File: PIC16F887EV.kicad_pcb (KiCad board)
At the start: 2 copper layers, 45 parts, among them J1 Conn_01x05_Socket, P1 USB_C_Plug_USB2.0, SW1 SW_Push, SW10 SW_Push, SW11 SW_Push, SW12 SW_Push, SW13 SW_Push, SW14 SW_Push, SW15 SW_Push, SW16 SW_Push, SW2 SW_Push, SW3 SW_Push, SW4 SW_Push, SW5 SW_Push, SW6 SW_Push, SW7 SW_Push, SW8 SW_Push, SW9 SW_Push, U1 PIC16F887-IP, U2 FT230XS, U3 MMBT2222A-7-F

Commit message: Displays
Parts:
- added R7: 10K, Resistor_SMD:R_1206_3216Metric_Pad1.30x1.75mm_HandSolder, F.Cu at (110.2, 116.1)
- added R8: 10K, Resistor_SMD:R_1206_3216Metric_Pad1.30x1.75mm_HandSolder, F.Cu at (110.2, 119.4)
- added RV1: R_Potentiometer, Potentiometer_SMD:Potentiometer_ACP_CA6-VSMD_Vertical, F.Cu at (132.1, 124.5)
- added SW17: SW_Push, Button_Switch_SMD:SW_Push_1P1T_NO_6x6mm_H9.5mm, F.Cu at (101.7, 118.2)
- added SW18: SW_Push, Button_Switch_SMD:SW_Push_1P1T_NO_6x6mm_H9.5mm, F.Cu at (101.7, 125.8)
- moved J1 18.5 mm to (142.2, 33.0)
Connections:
- U1 pad 6: unconnected-(U1-C1OUT/T0CKI/RA4-Pad6) -> RA4
- U1 pad 7: unconnected-(U1-C2OUT/~{SS}/AN4/RA5-Pad7) -> RA5

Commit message: Actualización
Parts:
- added AFF1: LTS-6980HR, Display_7Segment:7SegmentLED_LTS6760_LTS6780, F.Cu at (21.5, 71.5)
- added AFF2: LTS-6960HR, Display_7Segment:7SegmentLED_LTS6760_LTS6780, F.Cu at (21.5, 85.6)
- added AFF3: LTS-6980HR, Display_7Segment:7SegmentLED_LTS6760_LTS6780, F.Cu at (21.5, 99.8)
- added AFF4: LTS-6980HR, Display_7Segment:7SegmentLED_LTS6760_LTS6780, F.Cu at (21.5, 113.9)
- added JP1: Jumper_2_Bridged, Jumper:SolderJumper-2_P1.3mm_Bridged2Bar_Pad1.0x1.5mm, F.Cu at (41.6, 107.6)
- added Q1: 2N3904, Package_TO_SOT_THT:TO-92_Inline, F.Cu at (41.4, 72.7)
- added Q2: 2N3904, Package_TO_SOT_THT:TO-92_Inline, F.Cu at (41.4, 78.5)
- added Q3: 2N3904, Package_TO_SOT_THT:TO-92_Inline, F.Cu at (41.4, 84.3)
- added Q4: 2N3906, Package_TO_SOT_THT:TO-92_Inline, F.Cu at (41.4, 90.1)
- added RD12: 4.7k, Resistor_SMD:R_1206_3216Metric_Pad1.30x1.75mm_HandSolder, F.Cu at (42.4, 104.1)
- added RD4: 4.7k, Resistor_SMD:R_1206_3216Metric_Pad1.30x1.75mm_HandSolder, F.Cu at (42.4, 94.3)
- added RD5: 4.7k, Resistor_SMD:R_1206_3216Metric_Pad1.30x1.75mm_HandSolder, F.Cu at (42.4, 97.6)
- added RD6: 4.7k, Resistor_SMD:R_1206_3216Metric_Pad1.30x1.75mm_HandSolder, F.Cu at (42.4, 100.8)
- added Ra1: 200R, Resistor_SMD:R_1206_3216Metric_Pad1.30x1.75mm_HandSolder, F.Cu at (48.4, 94.3)
- added Ra2: 200R, Resistor_SMD:R_1206_3216Metric_Pad1.30x1.75mm_HandSolder, F.Cu at (48.4, 97.6)
- added Ra3: 200R, Resistor_SMD:R_1206_3216Metric_Pad1.30x1.75mm_HandSolder, F.Cu at (48.4, 100.8)
- added Ra4: 200R, Resistor_SMD:R_1206_3216Metric_Pad1.30x1.75mm_HandSolder, F.Cu at (48.4, 104.1)
- added Ra5: 200R, Resistor_SMD:R_1206_3216Metric_Pad1.30x1.75mm_HandSolder, F.Cu at (54.3, 94.3)
- added Ra6: 200R, Resistor_SMD:R_1206_3216Metric_Pad1.30x1.75mm_HandSolder, F.Cu at (54.3, 97.6)
- added Ra7: 200R, Resistor_SMD:R_1206_3216Metric_Pad1.30x1.75mm_HandSolder, F.Cu at (54.3, 100.8)
- added Ra8: 200R, Resistor_SMD:R_1206_3216Metric_Pad1.30x1.75mm_HandSolder, F.Cu at (54.3, 104.1)
- moved U1 5.08 mm to (129.5, 61.0)
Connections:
- SW1 pad 1: RD0 -> RB4
- SW10 pad 1: RD1 -> RB5
- SW11 pad 1: RD2 -> ICSPCLK
- SW12 pad 1: RD3 -> ICSPDAT
- SW13 pad 1: RD0 -> RB4
- SW14 pad 1: RD1 -> RB5
- SW15 pad 1: RD2 -> ICSPCLK
- SW16 pad 1: RD3 -> ICSPDAT
- SW2 pad 1: RD1 -> RB5
- SW3 pad 1: RD2 -> ICSPCLK
- SW4 pad 1: RD3 -> ICSPDAT
- SW5 pad 1: RD0 -> RB4
- SW6 pad 1: RD1 -> RB5
- SW7 pad 1: RD2 -> ICSPCLK
- SW8 pad 1: RD3 -> ICSPDAT
- SW9 pad 1: RD0 -> RB4
- U1 pad 10: unconnected-(U1-RE2/AN7-Pad10) -> RE2
- U1 pad 27: unconnected-(U1-RD4-Pad27) -> RD4
- U1 pad 28: unconnected-(U1-RD5/P1B-Pad28) -> RD5
- U1 pad 29: unconnected-(U1-RD6/P1C-Pad29) -> RD6
- U1 pad 30: unconnected-(U1-RD7/P1D-Pad30) -> RD7
- U1 pad 37: unconnected-(U1-AN11/RB4-Pad37) -> RB4
- U1 pad 38: unconnected-(U1-~{T1G}/AN13/RB5-Pad38) -> RB5
- U1 pad 8: unconnected-(U1-RE0/AN5-Pad8) -> RE0
- U1 pad 9: unconnected-(U1-RE1/AN6-Pad9) -> RE1

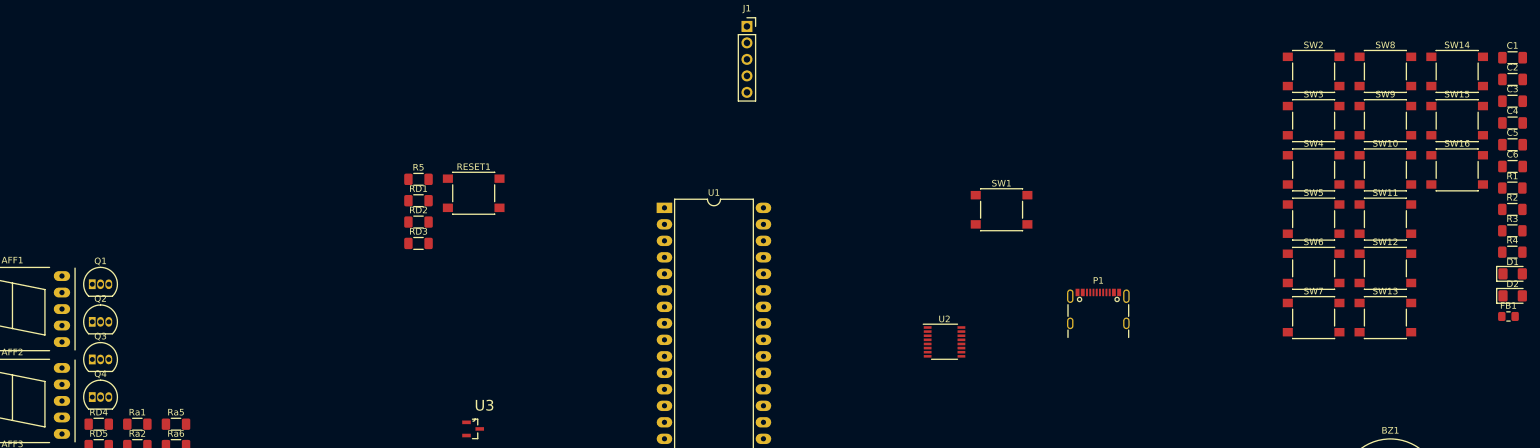
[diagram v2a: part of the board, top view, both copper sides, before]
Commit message: Actualizacion Puente + Huellas
Agregue componentes de interfaz entre PIC (5V) y puente USB (3V3).
Cambie las huellas de transistores a SMD.
Cambie el BJT 2N2222 por un 3904
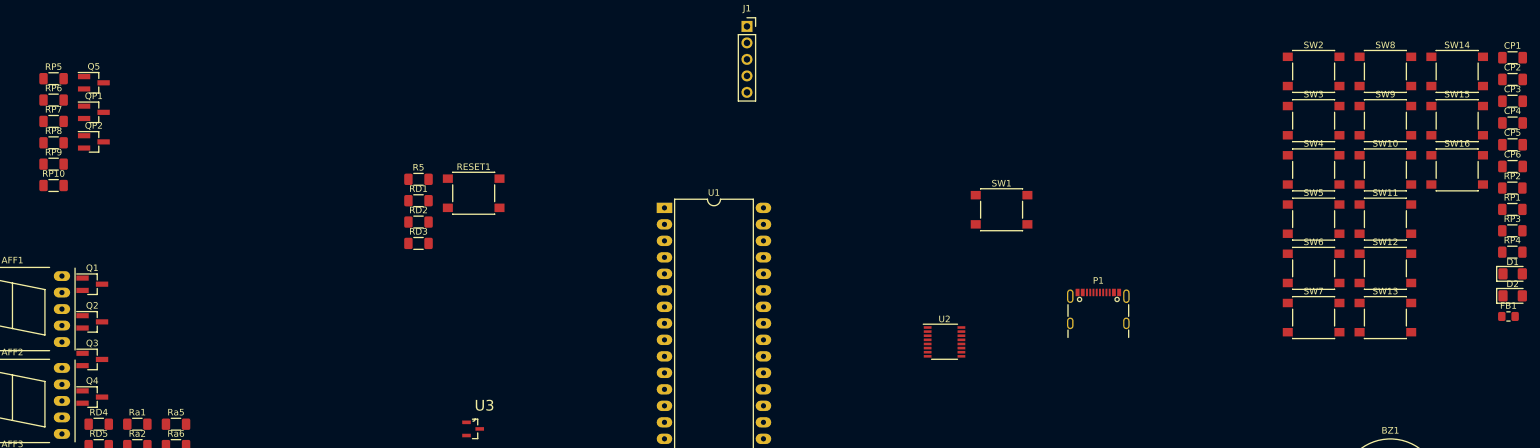
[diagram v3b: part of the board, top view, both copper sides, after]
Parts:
- added Q5: 2N3904, Package_TO_SOT_SMD:SOT-23_Handsoldering, F.Cu at (41.7, 41.7)
- added QP1: 2N3904, Package_TO_SOT_SMD:SOT-23_Handsoldering, F.Cu at (41.7, 46.2)
- added QP2: 2N3904, Package_TO_SOT_SMD:SOT-23_Handsoldering, F.Cu at (41.7, 50.8)
- added RP10: 10K, Resistor_SMD:R_1206_3216Metric_Pad1.30x1.75mm_HandSolder, F.Cu at (35.5, 57.5)
- added RP5: 2K2, Resistor_SMD:R_1206_3216Metric_Pad1.30x1.75mm_HandSolder, F.Cu at (35.5, 41.1)
- added RP6: 3K3, Resistor_SMD:R_1206_3216Metric_Pad1.30x1.75mm_HandSolder, F.Cu at (35.5, 44.4)
- added RP7: 4K7, Resistor_SMD:R_1206_3216Metric_Pad1.30x1.75mm_HandSolder, F.Cu at (35.5, 47.6)
- added RP8: 10K, Resistor_SMD:R_1206_3216Metric_Pad1.30x1.75mm_HandSolder, F.Cu at (35.5, 50.9)
- added RP9: 1K, Resistor_SMD:R_1206_3216Metric_Pad1.30x1.75mm_HandSolder, F.Cu at (35.5, 54.2)
- Q1, Q2, Q3, Q4: footprint Package_TO_SOT_THT:TO-92_Inline -> Package_TO_SOT_SMD:SOT-23_Handsoldering
- renumbered C1 to CP1, C2 to CP2, C3 to CP3, C4 to CP4, C5 to CP5, C6 to CP6, R2 to RP1, R1 to RP2, R3 to RP3, R4 to RP4
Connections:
- net Net-(D1-A) renamed +3.3V
- R6 pad 1: Net-(U3-B) -> Net-(Q5-B)
- U2 pad 1: RXpic -> Net-(U2-TXD)
- U2 pad 4: TXpic -> Net-(U2-RXD)

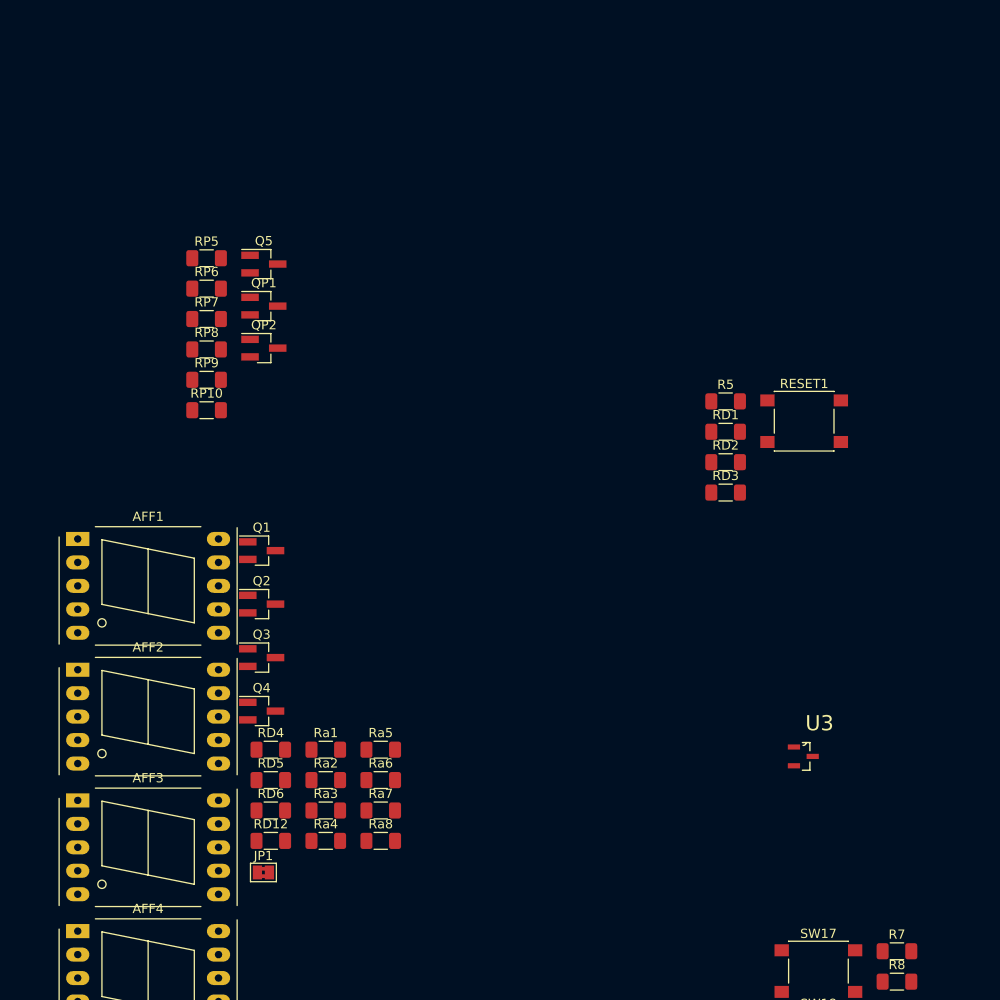
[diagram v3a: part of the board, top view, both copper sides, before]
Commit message: LimitesPCB+Reglas
Agregado el cuadrado de 10cmx10cm y algunas reglas de enrutamiento
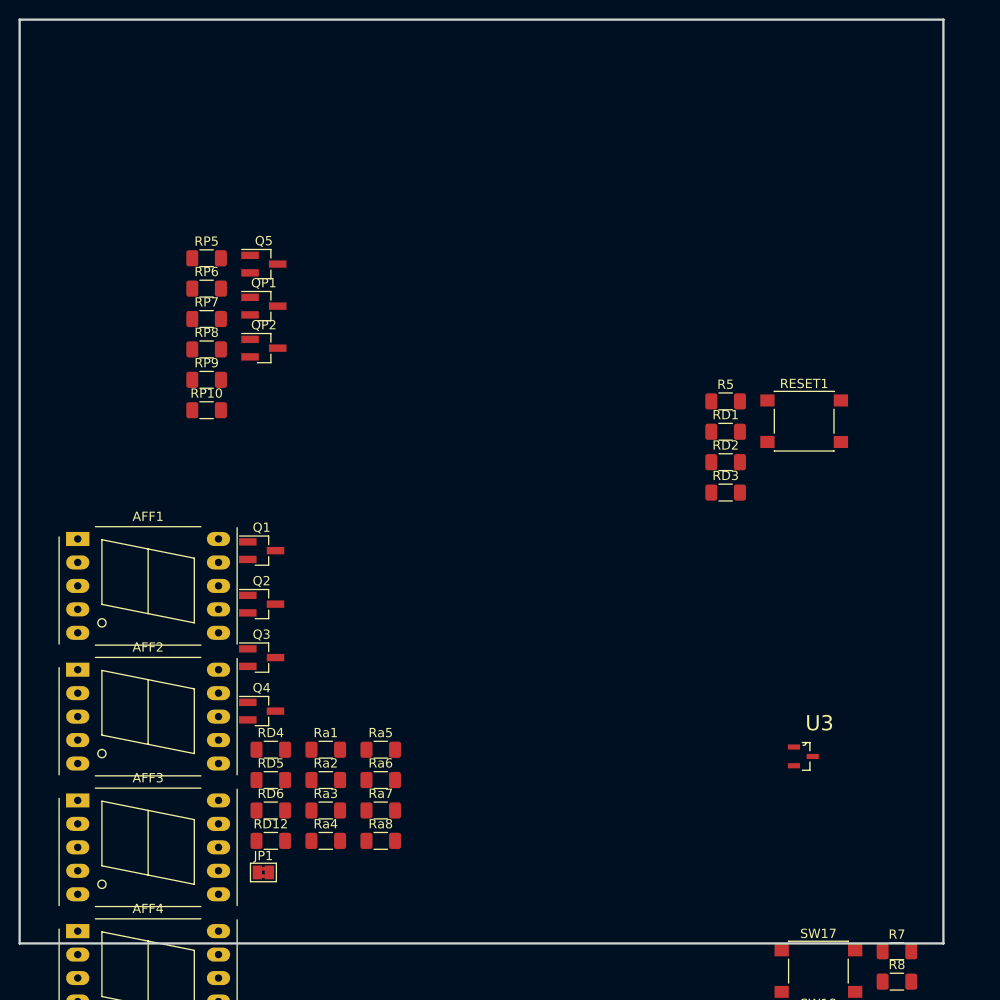
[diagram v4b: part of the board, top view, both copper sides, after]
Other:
- board outline added: 100 x 100 mm
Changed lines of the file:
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@@
     )
   )
+  (gr_rect locked (start 15.24 15.24) (end 115.24 115.24)
+    (stroke (width 0.25) (type solid)) (fill none) (layer "Edge.Cuts"))
 )

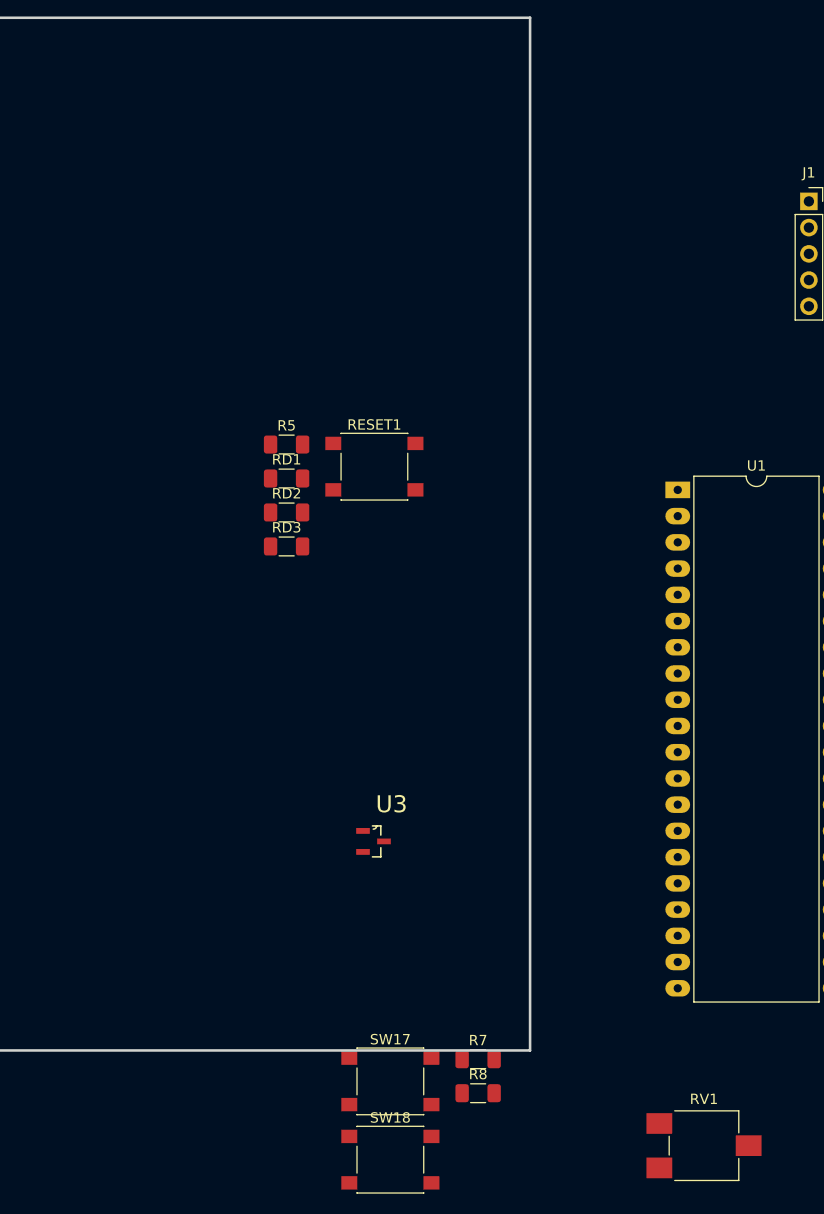
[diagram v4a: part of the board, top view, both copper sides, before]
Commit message: Avance esquemático
Cristal externo + Teclado en puertos A y B con pulldown + huella potenciometro + pin de programación
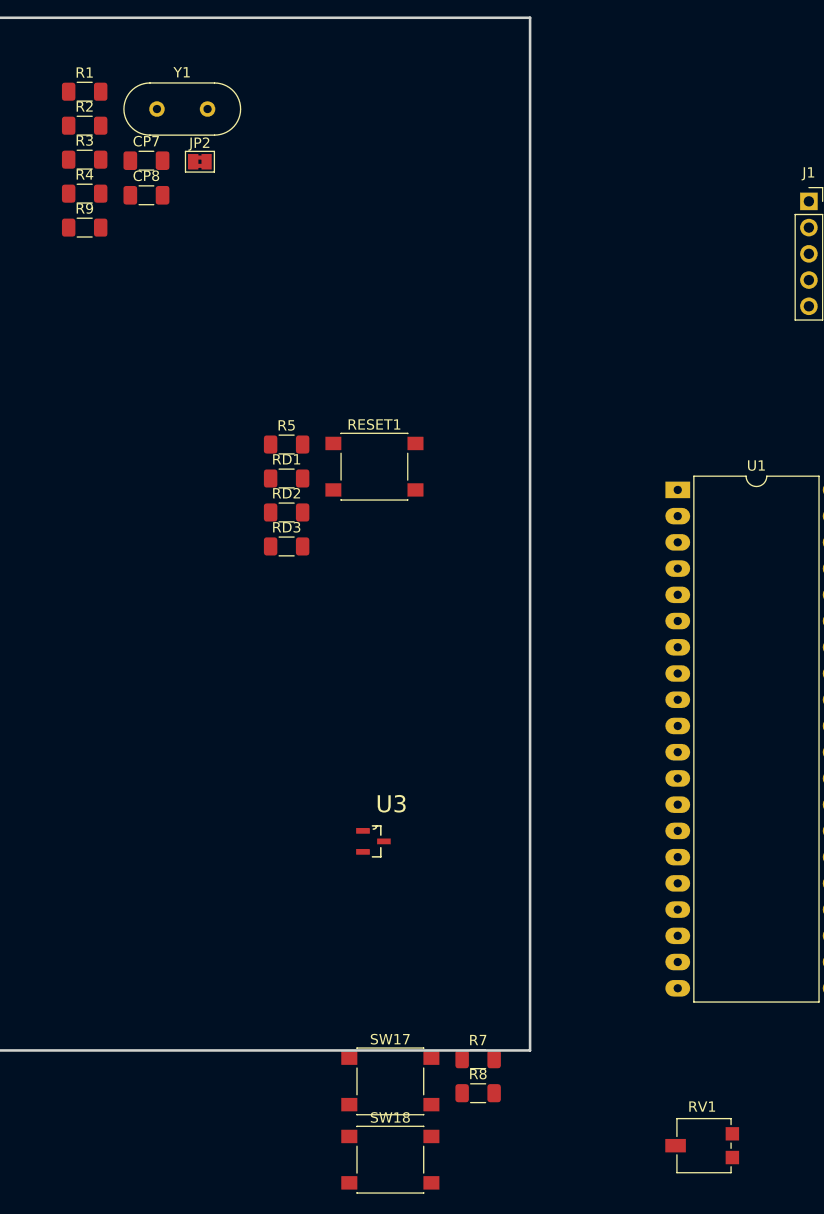
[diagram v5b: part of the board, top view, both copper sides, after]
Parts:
- added CP7: 47pF, Capacitor_SMD:C_1206_3216Metric_Pad1.33x1.80mm_HandSolder, F.Cu at (78.1, 29.1)
- added CP8: 47pF, Capacitor_SMD:C_1206_3216Metric_Pad1.33x1.80mm_HandSolder, F.Cu at (78.1, 32.4)
- added JP2: Jumper_2_Bridged, Jumper:SolderJumper-2_P1.3mm_Bridged2Bar_Pad1.0x1.5mm, F.Cu at (83.3, 29.2)
- added R1: 10K, Resistor_SMD:R_1206_3216Metric_Pad1.30x1.75mm_HandSolder, F.Cu at (72.1, 22.4)
- added R2: 10K, Resistor_SMD:R_1206_3216Metric_Pad1.30x1.75mm_HandSolder, F.Cu at (72.1, 25.7)
- added R3: 10K, Resistor_SMD:R_1206_3216Metric_Pad1.30x1.75mm_HandSolder, F.Cu at (72.1, 29.0)
- added R4: 10K, Resistor_SMD:R_1206_3216Metric_Pad1.30x1.75mm_HandSolder, F.Cu at (72.1, 32.3)
- added R9: 10K, Resistor_SMD:R_1206_3216Metric_Pad1.30x1.75mm_HandSolder, F.Cu at (72.1, 35.6)
- added Y1: Crystal, Crystal:Crystal_HC18-U_Vertical, F.Cu at (79.1, 24.1)
- RV1: footprint Potentiometer_SMD:Potentiometer_ACP_CA6-VSMD_Vertical -> Potentiometer_SMD:Potentiometer_Vishay_TS53YL_Vertical
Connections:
- JP1 pad 2: RA0 -> RA5
- R6 pad 2: RA3 -> RA4
- R7 pad 1: RA4 -> RB4
- R8 pad 1: RA5 -> RB5
- SW1 pad 1: RB4 -> RA0
- SW10 pad 1: RB5 -> RA1
- SW11 pad 1: ICSPCLK -> RA2
- SW12 pad 1: ICSPDAT -> RA3
- SW13 pad 1: RB4 -> RA0
- SW14 pad 1: RB5 -> RA1
- SW15 pad 1: ICSPCLK -> RA2
- SW16 pad 1: ICSPDAT -> RA3
- SW17 pad 1: RA4 -> RB4
- SW18 pad 1: RA5 -> RB5
- SW2 pad 1: RB5 -> RA1
- SW3 pad 1: ICSPCLK -> RA2
- SW4 pad 1: ICSPDAT -> RA3
- SW5 pad 1: RB4 -> RA0
- SW6 pad 1: RB5 -> RA1
- SW7 pad 1: ICSPCLK -> RA2
- SW8 pad 1: ICSPDAT -> RA3
- SW9 pad 1: RB4 -> RA0
- U1 pad 13: unconnected-(U1-RA7/OSC1/CLKIN-Pad13) -> Net-(U1-RA7/OSC1/CLKIN)
- U1 pad 14: unconnected-(U1-RA6/OSC2/CLKOUT-Pad14) -> Net-(U1-RA6/OSC2/CLKOUT)
- U1 pad 24: unconnected-(U1-SDO/RC5-Pad24) -> Net-(JP2-B)
- U1 pad 3: unconnected-(U1-C12IN1-/AN1/RA1-Pad3) -> RA1
- U1 pad 4: unconnected-(U1-C2IN+/CVref/Vref-/AN2/RA2-Pad4) -> RA2

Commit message: Distribución de componentes dentro del rectángulo de 10x10cm
Moví los componentes y los agrupé aproximadamente donde podrían ir dejando el PIC y el puente USB del lado inferior.
A los switchs de teclado les cambié la huella por una con modelo 3d pero del mismo footprint
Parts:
- removed AFF2: LTS-6960HR, Display_7Segment:7SegmentLED_LTS6760_LTS6780
- removed Q4: 2N3906, Package_TO_SOT_SMD:SOT-23_Handsoldering
- removed RD6: 4.7k, Resistor_SMD:R_1206_3216Metric_Pad1.30x1.75mm_HandSolder
- removed U3: MMBT2222A-7-F, Downloads:SOT103P240X110-3N
- CP1, CP2, CP3, CP4, CP5, CP6, D1, D2, FB1, P1, QP1, QP2, RP1, RP10, RP2, RP3, RP4, RP5, RP6, RP7, RP8, RP9, U1, U2: moved to B.Cu
- RESET1: footprint Button_Switch_SMD:SW_Push_1P1T_NO_6x6mm_H9.5mm -> Button_Switch_SMD:SW_SPST_TL3342
- SW1, SW10, SW11, SW12, SW13, SW14, SW15, SW16, SW17, SW18, SW2, SW3, SW4, SW5, SW6, SW7, SW8, SW9: footprint Button_Switch_SMD:SW_Push_1P1T_NO_6x6mm_H9.5mm -> Button_Switch_SMD:SW_SPST_PTS645
- moved CP3 233.5 mm to (27.4, 63.3), turned to -90 degrees
- moved CP2 233.1 mm to (27.4, 55.3), turned to 90 degrees
- moved SW14 229.9 mm to (32.5, 109.6)
- moved CP1 229.6 mm to (31.9, 63.3), turned to 90 degrees
- moved FB1 229.4 mm to (30.9, 58.8)
- moved RP1 226.4 mm to (33.9, 51.5)
- moved RP2 226.2 mm to (33.9, 54.8)
- moved SW9 225.1 mm to (21.5, 99.6)
- moved CP4 224.6 mm to (36.3, 66.7)
- moved CP5 224.1 mm to (36.3, 63.3)
- moved CP6 223.8 mm to (36.3, 60.0)
- moved SW13 221.3 mm to (21.5, 109.6)
- moved SW15 217.6 mm to (43.0, 109.6)
- moved RP4 217.3 mm to (43.4, 52.0)
- moved RP3 216.9 mm to (43.4, 55.3)
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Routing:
- net TXpic: track 0.00 -> 1.00 mm
